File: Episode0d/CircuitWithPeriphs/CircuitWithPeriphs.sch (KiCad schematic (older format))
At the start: 0 parts

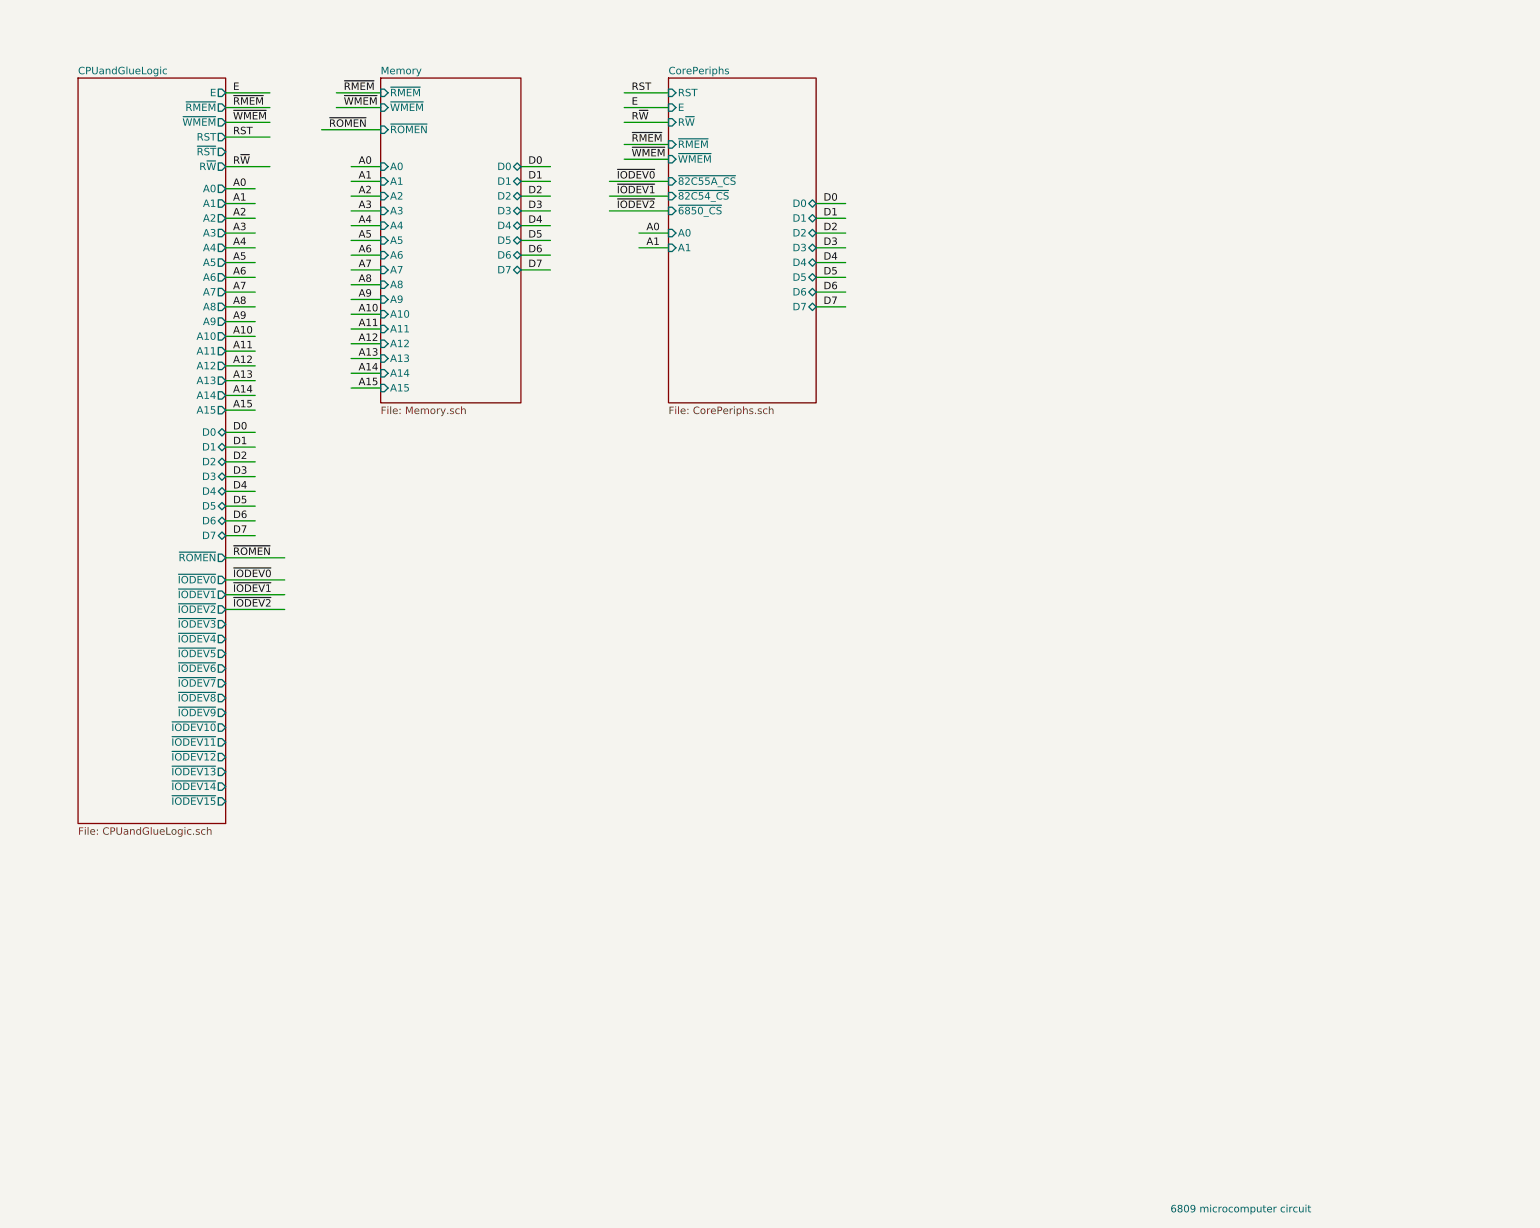
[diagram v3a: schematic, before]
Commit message: show ACIA connections to FT232RL breakout
Use current-limiting resistors between ACIA and FT232RL,
since they are powered by different sources, and we don't
want current flow between them.  (Got this idea from
Grant Searle's minimal 6809 project.)  Not sure if the
FT232RL should have its VCC connected to the 6809 system's
VCC: need to check old prototype.
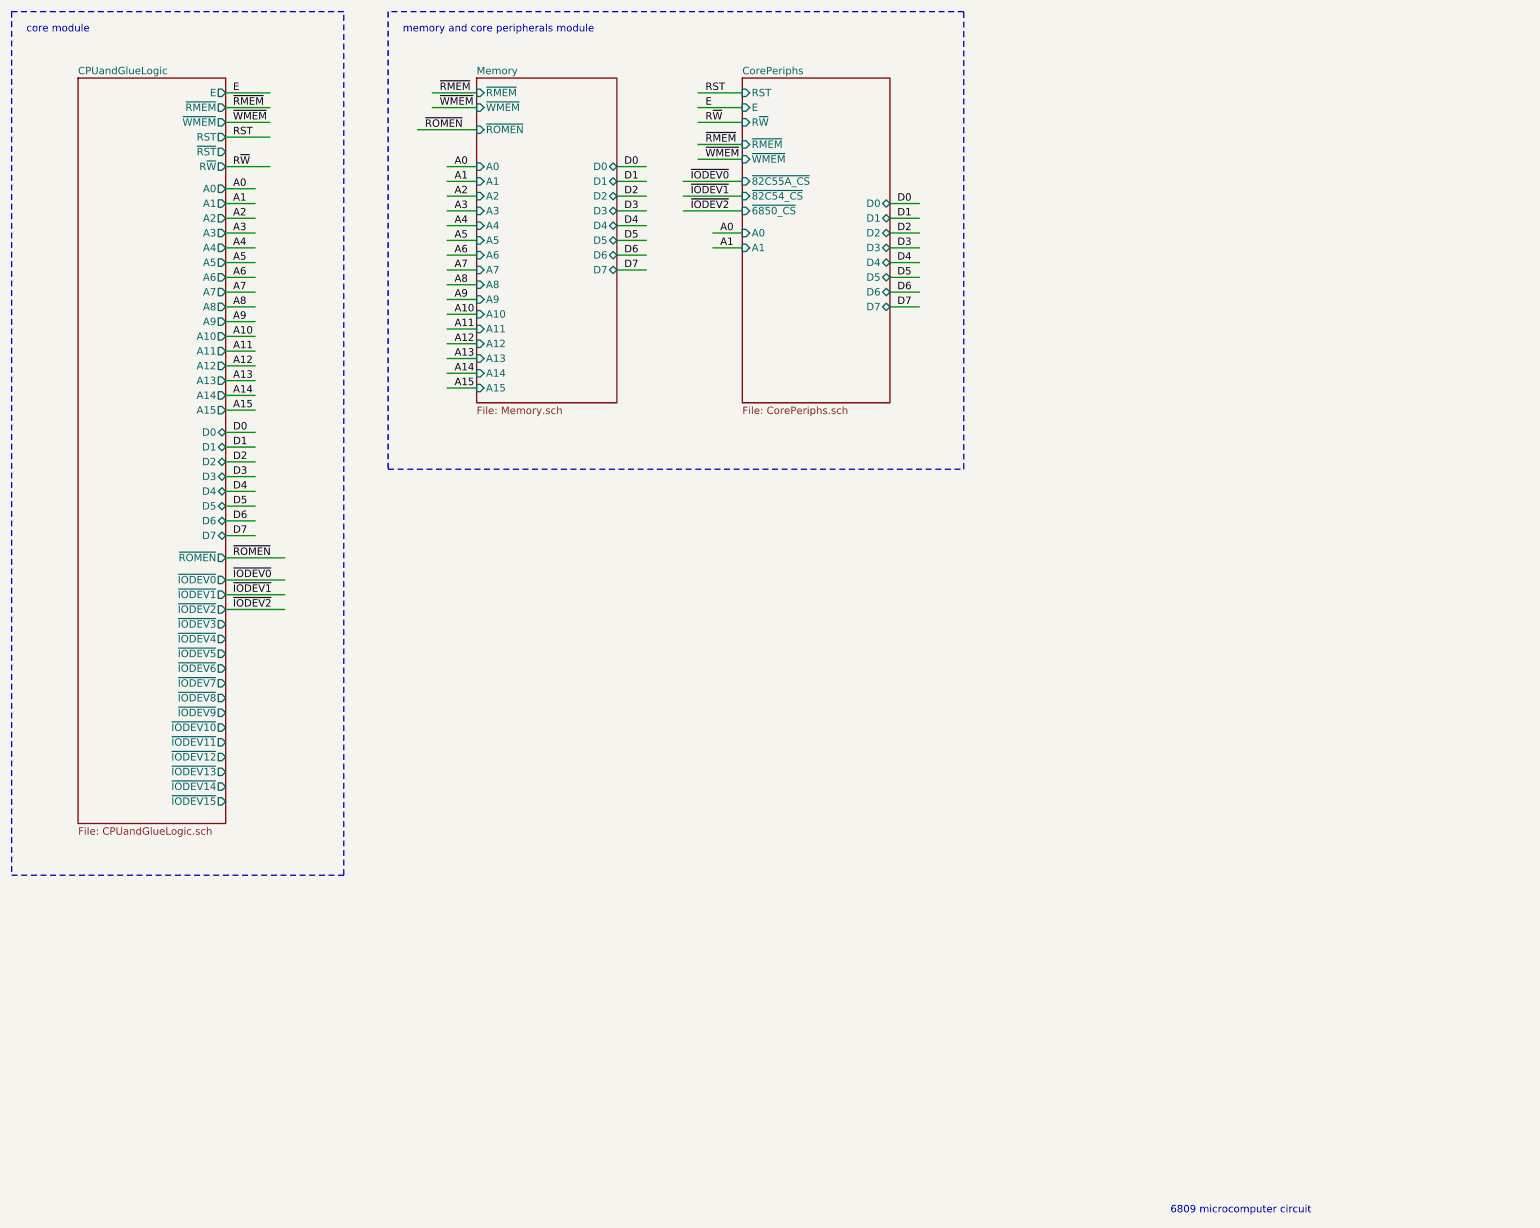
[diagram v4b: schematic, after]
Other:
- note added: "core module"
- note added: "memory and core peripherals module"
